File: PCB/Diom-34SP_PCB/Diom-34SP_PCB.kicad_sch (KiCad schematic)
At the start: 30 parts, among them J1 Conn_01x02_Male, U1 nice_nano

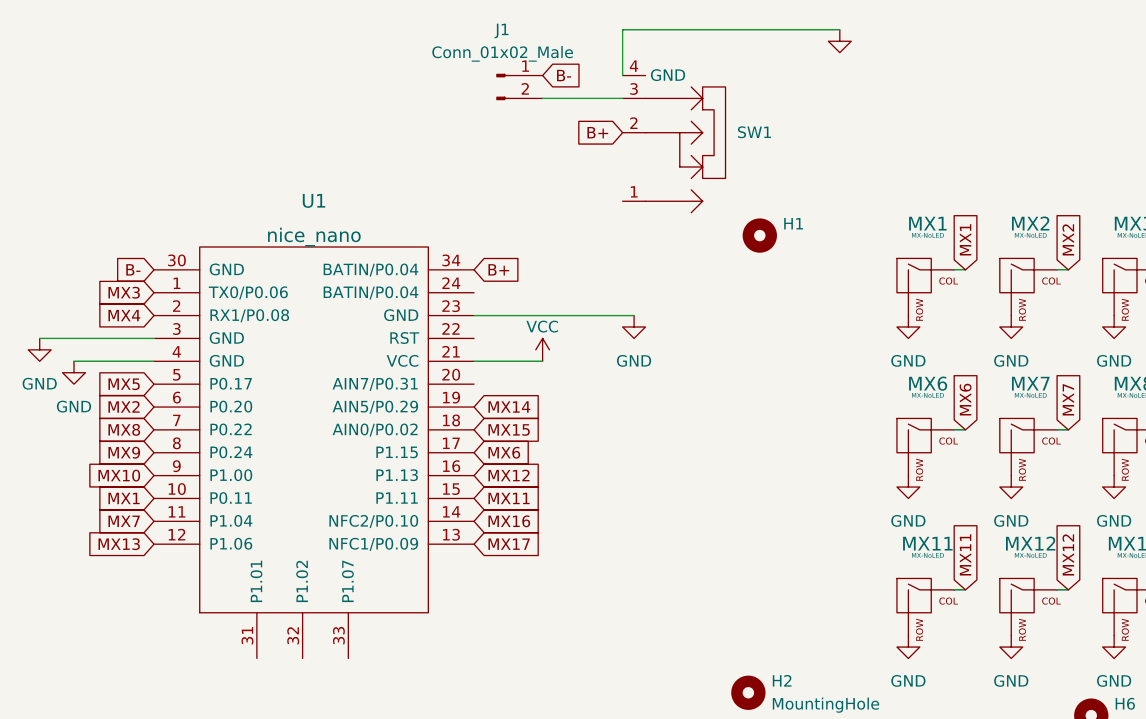
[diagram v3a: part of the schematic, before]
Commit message: Moved Artwork, Tracks, Rounded PCB
Also Gerbers
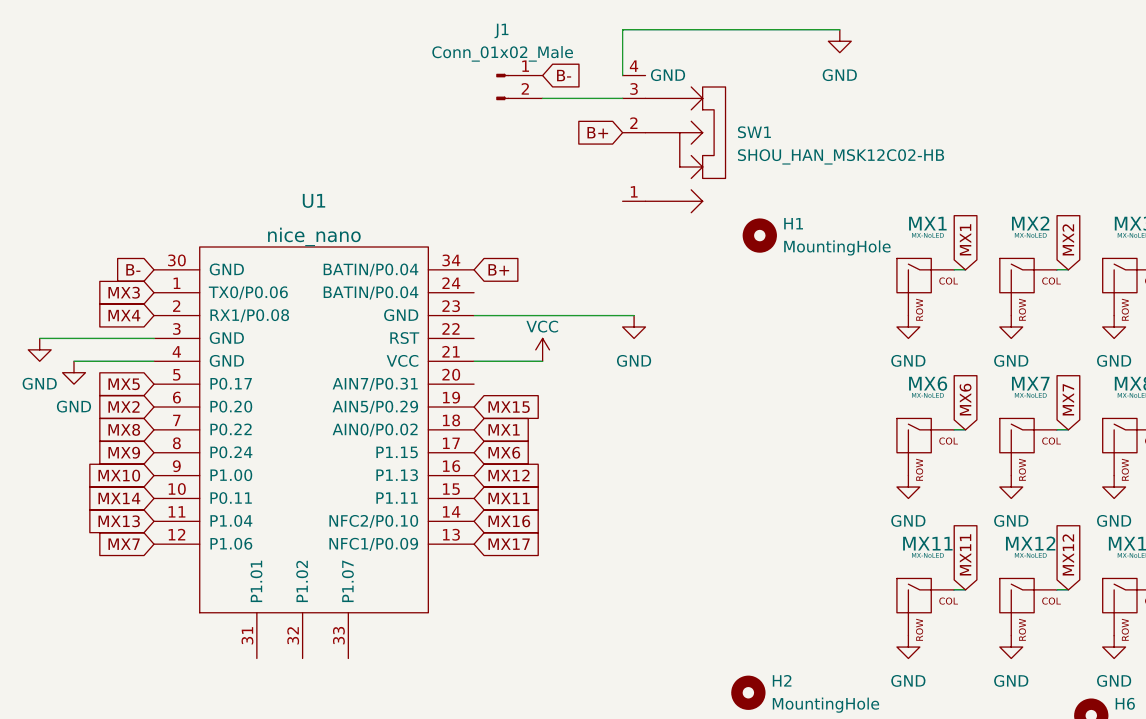
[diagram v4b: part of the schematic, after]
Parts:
- H1: value (none) -> MountingHole; footprint (none) -> MountingHole:MountingHole_2.2mm_M2_DIN965
- SW1: value (none) -> SHOU_HAN_MSK12C02-HB; footprint (none) -> led:SHOU HAN MSK12C02-HB
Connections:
- net MX1: now also U1.18 (AIN0/P0.02); no longer U1.10 (P0.11)
- net MX13: now also U1.11 (P1.04); no longer U1.12 (P1.06)
- net MX14: now also U1.10 (P0.11); no longer U1.19 (AIN5/P0.29)
- net MX15: now also U1.19 (AIN5/P0.29); no longer U1.18 (AIN0/P0.02)
- net MX7: now also U1.12 (P1.06); no longer U1.11 (P1.04)
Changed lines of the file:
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@@
     )
   )
-  (global_label "MX1" (shape input) (at 55.88 64.77 180) (fields_autoplaced)
+  (global_label "MX1" (shape input) (at 91.44 57.15 0) (fields_autoplaced)
+    (effects (font (size 1.27 1.27)) (justify left))
+    (property "Intersheet References" "${INTERSHEET_REFS}" (id 0) (at 97.7236 57.0706 0)
+      (effects (font (size 1.27 1.27)) (justify left) hide)
+    )
+  )
+  (global_label "MX10" (shape input) (at 191.77 57.15 90) (fields_autoplaced)
+    (effects (font (size 1.27 1.27)) (justify left))
+    (property "Intersheet References" "${INTERSHEET_REFS}" (id 0) (at 191.6906 49.6569 90)
+      (effects (font (size 1.27 1.27)) (justify left) hide)
+    )
+  )
+  (global_label "MX14" (shape input) (at 180.34 74.93 90) (fields_autoplaced)
+    (effects (font (size 1.27 1.27)) (justify left))
+    (property "Intersheet References" "${INTERSHEET_REFS}" (id 0) (at 180.2606 67.4369 90)
+      (effects (font (size 1.27 1.27)) (justify left) hide)
+    )
+  )
+  (global_label "MX14" (shape input) (at 55.88 64.77 180) (fields_autoplaced)
     (effects (font (size 1.27 1.27)) (justify right))
-    (property "Intersheet References" "${INTERSHEET_REFS}" (id 0) (at 49.5964 64.8494 0)
+    (property "Intersheet References" "${INTERSHEET_REFS}" (id 0) (at 48.3869 64.8494 0)
       (effects (font (size 1.27 1.27)) (justify right) hide)
     )
   )
-  (global_label "MX10" (shape input) (at 191.77 57.15 90) (fields_autoplaced)
-    (effects (font (size 1.27 1.27)) (justify left))
-    (property "Intersheet References" "${INTERSHEET_REFS}" (id 0) (at 191.6906 49.6569 90)
-      (effects (font (size 1.27 1.27)) (justify left) hide)
-    )
-  )
-  (global_label "MX14" (shape input) (at 180.34 74.93 90) (fields_autoplaced)
-    (effects (font (size 1.27 1.27)) (justify left))
-    (property "Intersheet References" "${INTERSHEET_REFS}" (id 0) (at 180.2606 67.4369 90)
-      (effects (font (size 1.27 1.27)) (justify left) hide)
-    )
-  )
-  (global_label "MX14" (shape input) (at 91.44 54.61 0) (fields_autoplaced)
-    (effects (font (size 1.27 1.27)) (justify left))
-    (property "Intersheet References" "${INTERSHEET_REFS}" (id 0) (at 98.9331 54.5306 0)
-      (effects (font (size 1.27 1.27)) (justify left) hide)
-    )
-  )
   (global_label "MX3" (shape input) (at 168.91 39.37 90) (fields_autoplaced)
     (effects (font (size 1.27 1.27)) (justify left))
@@
     )
   )
-  (global_label "MX13" (shape input) (at 55.88 69.85 180) (fields_autoplaced)
+  (global_label "MX13" (shape input) (at 55.88 67.31 180) (fields_autoplaced)
     (effects (font (size 1.27 1.27)) (justify right))
-    (property "Intersheet References" "${INTERSHEET_REFS}" (id 0) (at 48.3869 69.9294 0)
+    (property "Intersheet References" "${INTERSHEET_REFS}" (id 0) (at 48.3869 67.3894 0)
       (effects (font (size 1.27 1.27)) (justify right) hide)
     )
@@
     )
   )
-  (global_label "MX7" (shape input) (at 55.88 67.31 180) (fields_autoplaced)
+  (global_label "MX7" (shape input) (at 55.88 69.85 180) (fields_autoplaced)
     (effects (font (size 1.27 1.27)) (justify right))
-    (property "Intersheet References" "${INTERSHEET_REFS}" (id 0) (at 49.5964 67.3894 0)
+    (property "Intersheet References" "${INTERSHEET_REFS}" (id 0) (at 49.5964 69.9294 0)
       (effects (font (size 1.27 1.27)) (justify right) hide)
     )
@@
     )
   )
-  (global_label "MX15" (shape input) (at 91.44 57.15 0) (fields_autoplaced)
-    (effects (font (size 1.27 1.27)) (justify left))
-    (property "Intersheet References" "${INTERSHEET_REFS}" (id 0) (at 98.9331 57.0706 0)
+  (global_label "MX15" (shape input) (at 91.44 54.61 0) (fields_autoplaced)
+    (effects (font (size 1.27 1.27)) (justify left))
+    (property "Intersheet References" "${INTERSHEET_REFS}" (id 0) (at 98.9331 54.5306 0)
       (effects (font (size 1.27 1.27)) (justify left) hide)
     )
@@
       (effects (font (size 1.27 1.27)) (justify right))
     )
-    (property "Value" "" (id 1) (at 120.65 26.6699 90)
+    (property "Value" "SHOU_HAN_MSK12C02-HB" (id 1) (at 120.65 26.6699 90)
       (effects (font (size 1.27 1.27)) (justify right))
     )
-    (property "Footprint" "" (id 2) (at 119.38 24.13 0)
+    (property "Footprint" "led:SHOU HAN MSK12C02-HB" (id 2) (at 119.38 24.13 0)
       (effects (font (size 1.27 1.27)) hide)
     )
@@
       (effects (font (size 1.27 1.27)) (justify left))
     )
-    (property "Value" "" (id 1) (at 125.73 36.8299 0)
-      (effects (font (size 1.27 1.27)) (justify left))
-    )
-    (property "Footprint" "" (id 2) (at 123.19 35.56 0)
+    (property "Value" "MountingHole" (id 1) (at 125.73 36.8299 0)
+      (effects (font (size 1.27 1.27)) (justify left))
+    )
+    (property "Footprint" "MountingHole:MountingHole_2.2mm_M2_DIN965" (id 2) (at 123.19 35.56 0)
       (effects (font (size 1.27 1.27)) hide)
     )
@@
       (effects (font (size 1.27 1.27)) hide)
     )
-    (property "Value" "" (id 1) (at 132.08 17.78 0))
+    (property "Value" "GND" (id 1) (at 132.08 17.78 0))
     (property "Footprint" "" (id 2) (at 132.08 12.7 0)
       (effects (font (size 1.27 1.27)) hide)

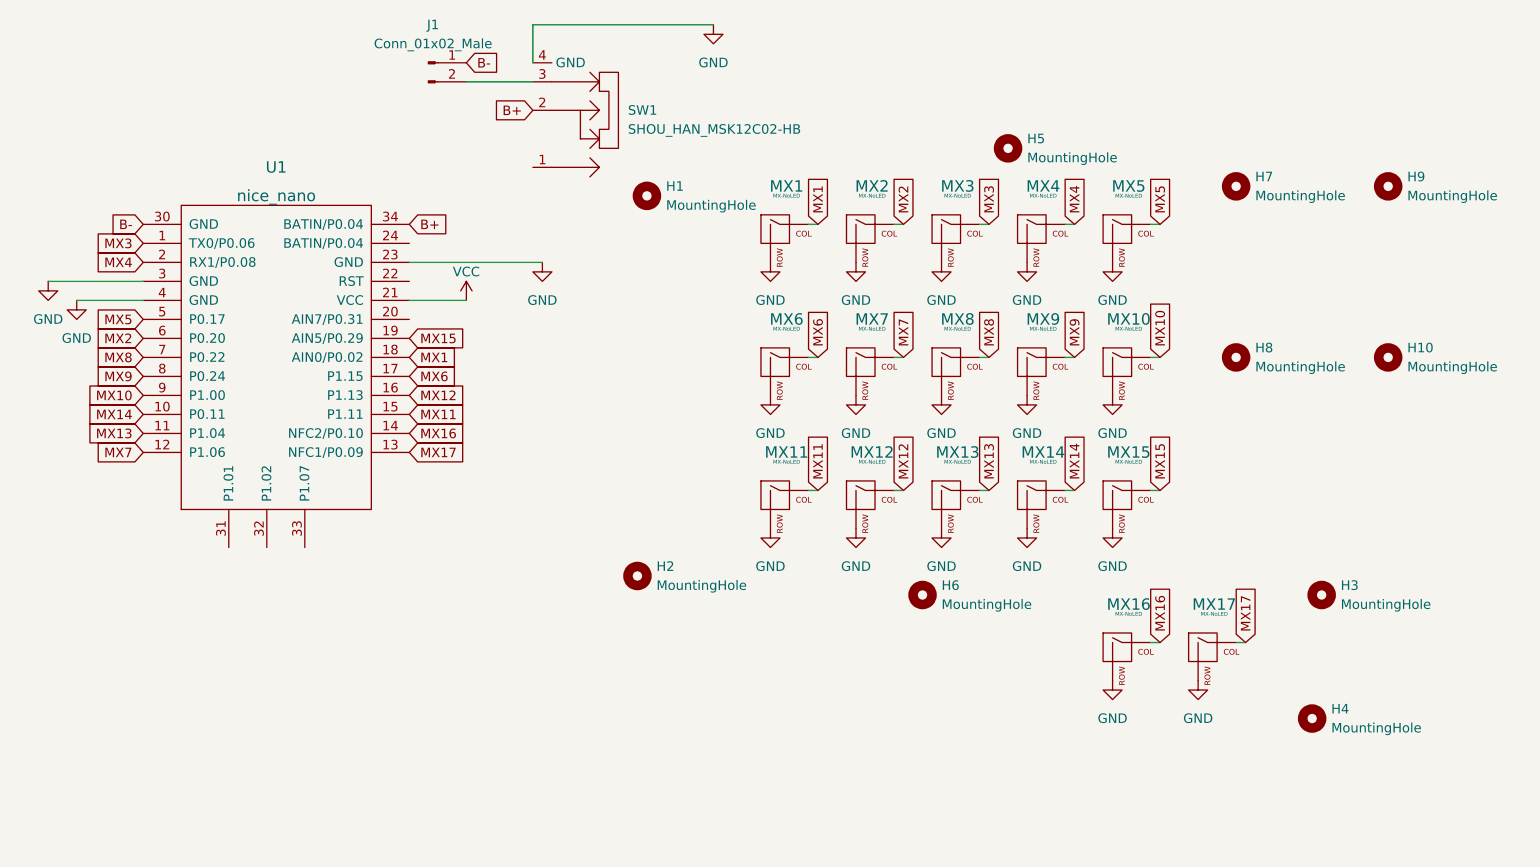
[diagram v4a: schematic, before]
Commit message: Massive Changes
-New Switch
-New Outline
-More Mounting Holes
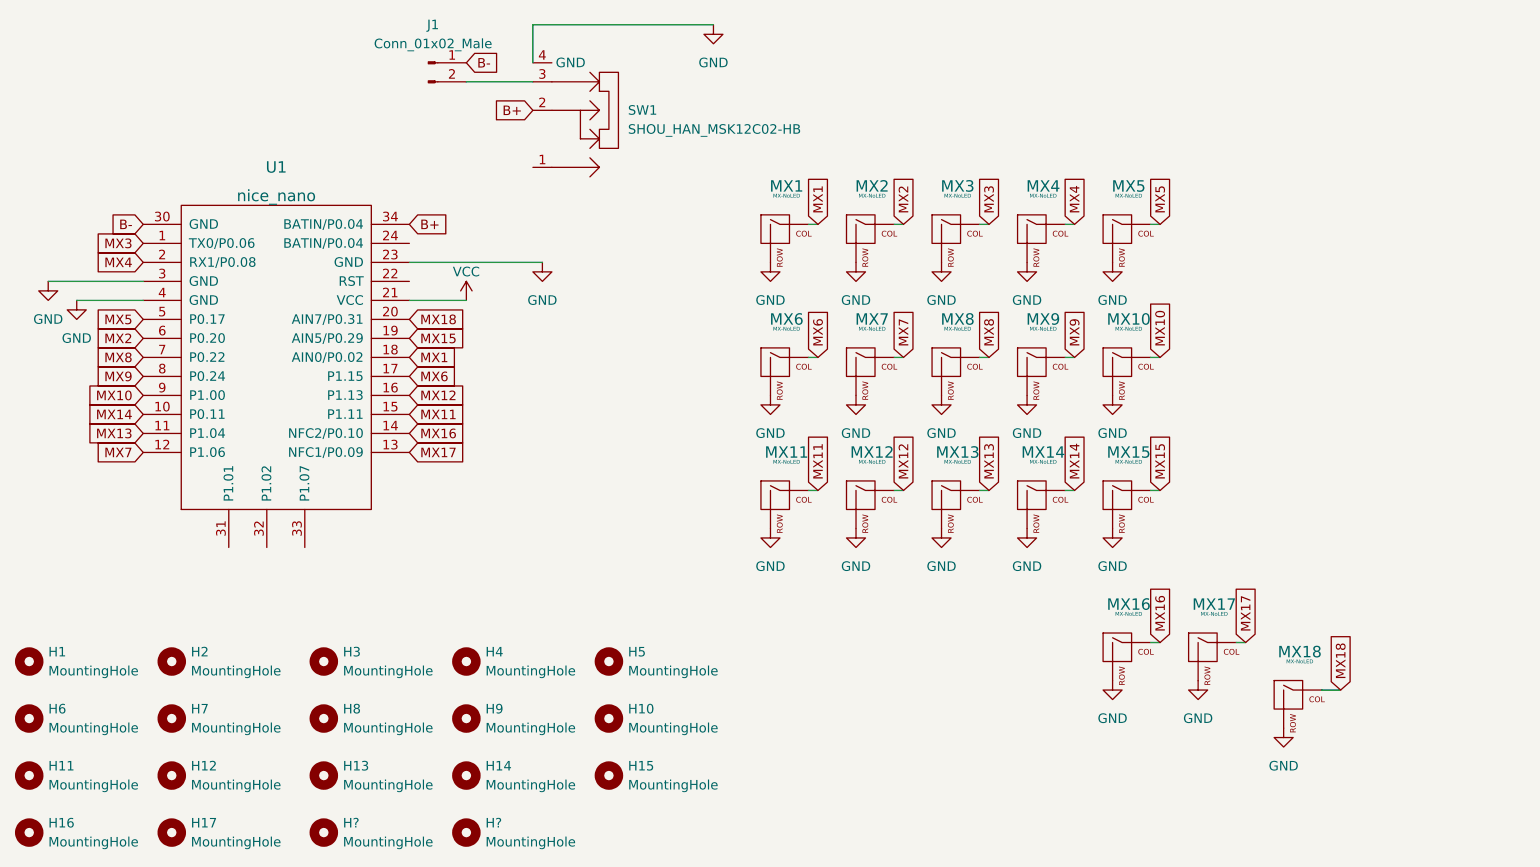
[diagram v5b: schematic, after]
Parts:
- added H11, H12, H13, H14, H15, H16, H17, H? (x2): MountingHole, MountingHole:MountingHole_2.2mm_M2_DIN965, symbol Mechanical:MountingHole
- added MX18: MX-NoLED, symbol MX_Alps_Hybrid:MX-NoLED
- MX1, MX10, MX11, MX12, MX13, MX14, MX15, MX16, MX2, MX3, MX4, MX5, MX6, MX7, MX8, MX9: footprint mx-switches-doubleSided:CherryMX-1U-doubleSided -> (none)
- MX17: footprint mx-switches-doubleSided:CherryMX-1.5U-doubleSided-Vertical -> (none)
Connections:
- net GND: now also MX18.2 (ROW)
- net MX18: now reaches U1.20 (AIN7/P0.31)
- net MX18: now also MX18.1 (COL)
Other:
- moved on the sheet: H1, H10, H2, H3, H4, H5, H6, H7, H8, H9
